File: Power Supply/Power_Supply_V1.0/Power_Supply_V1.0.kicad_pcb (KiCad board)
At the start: 2 copper layers, 158.8 x 67.3 mm, 44 parts

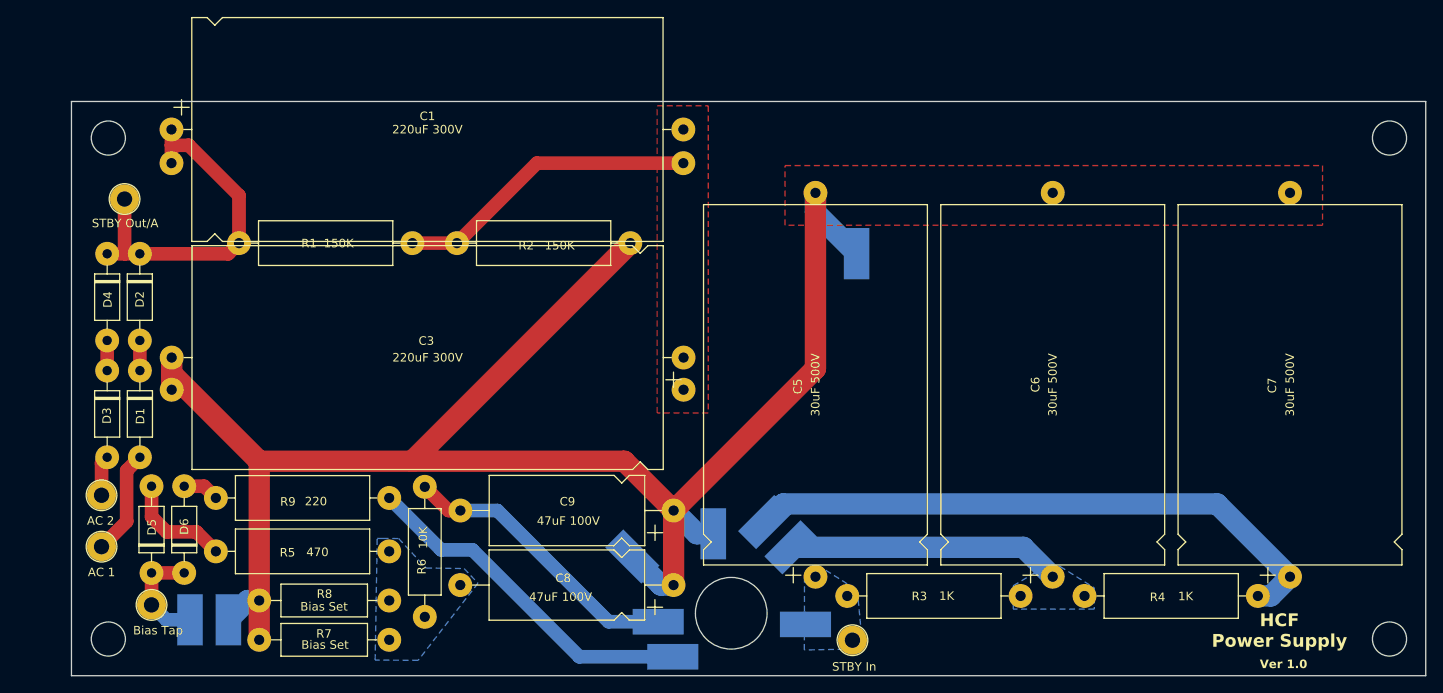
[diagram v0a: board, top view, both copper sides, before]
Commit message: increased trace width
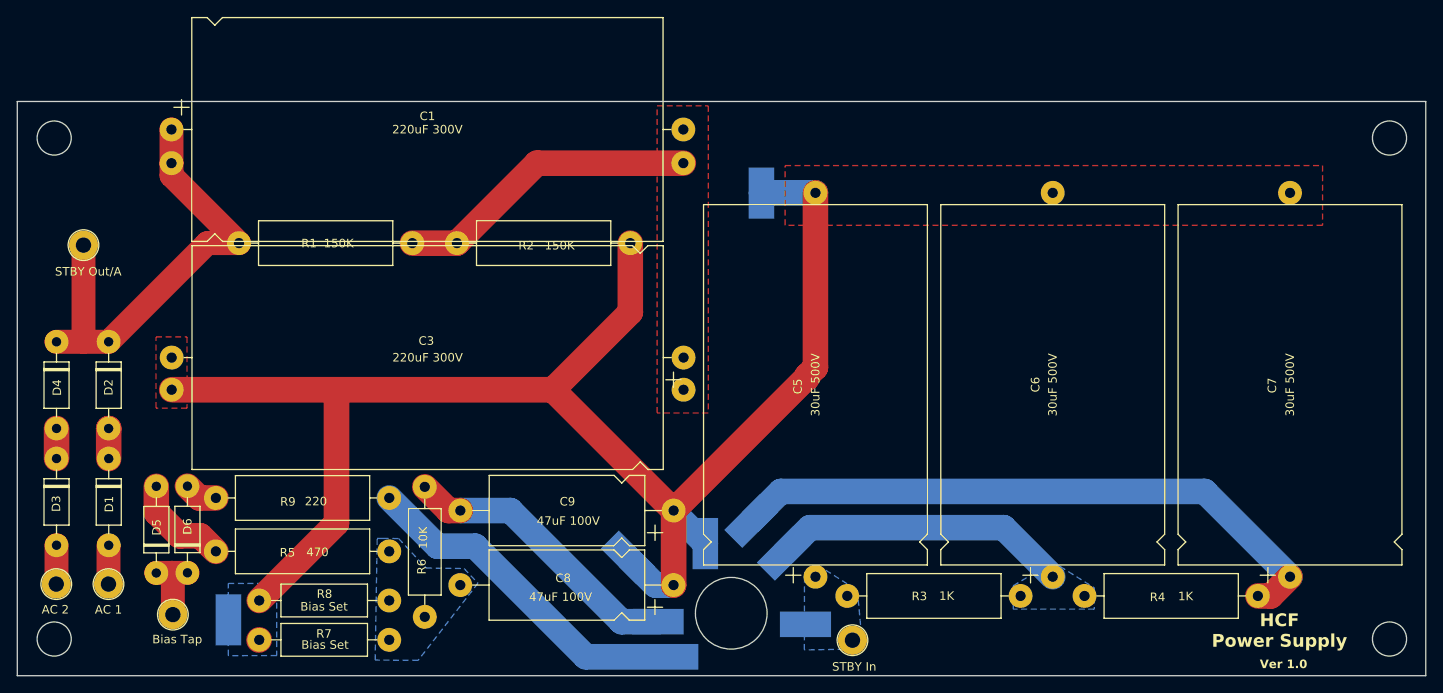
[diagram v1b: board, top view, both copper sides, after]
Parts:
- removed TP15: Bias Tap Out, HiroFootprints:WirePad
- moved TP14 13.2 mm to (142.2, 80.5)
- moved D3 11.9 mm to (59.6, 111.3)
- moved D4 11.9 mm to (59.6, 97.7)
- moved TP11 11.7 mm to (59.6, 126.1)
- moved D1 10.9 mm to (65.7, 111.3)
- moved D2 10.9 mm to (65.7, 97.7)
- moved TP1 7.24 mm to (62.8, 86.3)
- moved REF** 6.35 mm to (59.3, 73.8)
- moved REF** 6.35 mm to (59.3, 132.5)
- moved TP10 4.46 mm to (65.7, 126.1)
- moved TP9 2.75 mm to (73.2, 129.6)
- moved TP5 1.63 mm to (140.9, 118.8)
- moved TP12 1.49 mm to (135.7, 121.1)
- moved TP4 1.14 mm to (144.7, 122.7)
- moved D5 0.56 mm to (71.3, 124.8)
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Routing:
- net GND: track 204.9 -> 185.5 mm
- net Net-(D2-K): track 42.3 -> 54.1 mm
- net Net-(D1-A): track 12.3 -> 4.56 mm
- net 60VAC: track 12.8 -> 8.58 mm
- net C: track 32.1 -> 35.1 mm
- net D: track 70.6 -> 73.4 mm
- net Net-(D5-A): track 12.8 -> 11.9 mm
- added copper zone on B.Cu, net GND
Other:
- board size 158.8 x 67.3 mm -> 165.1 x 67.3 mm

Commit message: updated power supply board with more diode spacing
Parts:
- moved TP1 2.31 mm to (62.3, 88.6)
- moved TP9 0.94 mm to (72.5, 129.0)
- moved D5 0.93 mm to (70.4, 124.7)
- moved D6 0.40 mm to (74.5, 124.8)
- moved D4 0.28 mm to (59.3, 97.6)
- moved TP11 0.28 mm to (59.3, 126.0)
- moved D3 0.28 mm to (59.3, 111.3)
- moved D2 0.28 mm to (65.4, 97.6)
- moved TP10 0.28 mm to (65.4, 126.0)
- moved D1 0.28 mm to (65.5, 111.3)
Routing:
- net Net-(D2-K): track 54.1 -> 52.0 mm
- net Net-(D5-A): track 11.9 -> 13.1 mm
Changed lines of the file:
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@@
 	(footprint "HiroFootprints:Out_Hole_3.4_1.8"
 		(layer "F.Cu")
-		(at 65.69 126.06)
+		(at 65.42 126)
 		(property "Reference" "TP10"
 			(at 0 -0.5 0)
@@
 	(footprint "Diode_THT:D_DO-41_SOD81_P10.16mm_Horizontal"
 		(layer "F.Cu")
-		(at 59.6 97.66 -90)
+		(at 59.33 97.6 -90)
 		(descr "Diode, DO-41_SOD81 series, Axial, Horizontal, pin pitch=10.16mm, , length*diameter=5.2*2.7mm^2, , http://www.diodes.com/_files/packages/DO-41%20(Plastic).pdf")
 		(tags "Diode DO-41_SOD81 series Axial Horizontal pin pitch 10.16mm  length 5.2mm diameter 2.7mm")
@@
 	(footprint "Diode_THT:D_DO-41_SOD81_P10.16mm_Horizontal"
 		(layer "F.Cu")
-		(at 74.945625 124.74 90)
+		(at 74.55 124.75 90)
 		(descr "Diode, DO-41_SOD81 series, Axial, Horizontal, pin pitch=10.16mm, , length*diameter=5.2*2.7mm^2, , http://www.diodes.com/_files/packages/DO-41%20(Plastic).pdf")
 		(tags "Diode DO-41_SOD81 series Axial Horizontal pin pitch 10.16mm  length 5.2mm diameter 2.7mm")
@@
 	(footprint "Diode_THT:D_DO-41_SOD81_P10.16mm_Horizontal"
 		(layer "F.Cu")
-		(at 65.72 111.35 -90)
+		(at 65.45 111.29 -90)
 		(descr "Diode, DO-41_SOD81 series, Axial, Horizontal, pin pitch=10.16mm, , length*diameter=5.2*2.7mm^2, , http://www.diodes.com/_files/packages/DO-41%20(Plastic).pdf")
 		(tags "Diode DO-41_SOD81 series Axial Horizontal pin pitch 10.16mm  length 5.2mm diameter 2.7mm")
@@
 	(footprint "HiroFootprints:Out_Hole_3.4_1.8"
 		(layer "F.Cu")
-		(at 62.76 86.33)
+		(at 62.28 88.59)
 		(property "Reference" "TP1"
 			(at 0 -0.5 0)
@@
 	(footprint "Diode_THT:D_DO-41_SOD81_P10.16mm_Horizontal"
 		(layer "F.Cu")
-		(at 71.3 124.76 90)
+		(at 70.37 124.74 90)
 		(descr "Diode, DO-41_SOD81 series, Axial, Horizontal, pin pitch=10.16mm, , length*diameter=5.2*2.7mm^2, , http://www.diodes.com/_files/packages/DO-41%20(Plastic).pdf")
 		(tags "Diode DO-41_SOD81 series Axial Horizontal pin pitch 10.16mm  length 5.2mm diameter 2.7mm")
@@
 	(footprint "HiroFootprints:Out_Hole_3.4_1.8"
 		(layer "F.Cu")
-		(at 73.24 129.64)
+		(at 72.54 129.02)
 		(property "Reference" "TP9"
 			(at 0 -0.5 0)
@@
 	(footprint "Diode_THT:D_DO-41_SOD81_P10.16mm_Horizontal"
 		(layer "F.Cu")
-		(at 65.71 97.66 -90)
+		(at 65.44 97.6 -90)
 		(descr "Diode, DO-41_SOD81 series, Axial, Horizontal, pin pitch=10.16mm, , length*diameter=5.2*2.7mm^2, , http://www.diodes.com/_files/packages/DO-41%20(Plastic).pdf")
 		(tags "Diode DO-41_SOD81 series Axial Horizontal pin pitch 10.16mm  length 5.2mm diameter 2.7mm")
@@
 	(footprint "HiroFootprints:Out_Hole_3.4_1.8"
 		(layer "F.Cu")
-		(at 59.57 126.06)
+		(at 59.3 126)
 		(property "Reference" "TP11"
 			(at 0 -0.5 0)
@@
 	(footprint "Diode_THT:D_DO-41_SOD81_P10.16mm_Horizontal"
 		(layer "F.Cu")
-		(at 59.6 111.35 -90)
+		(at 59.33 111.29 -90)
 		(descr "Diode, DO-41_SOD81 series, Axial, Horizontal, pin pitch=10.16mm, , length*diameter=5.2*2.7mm^2, , http://www.diodes.com/_files/packages/DO-41%20(Plastic).pdf")
 		(tags "Diode DO-41_SOD81 series Axial Horizontal pin pitch 10.16mm  length 5.2mm diameter 2.7mm")
@@
 	)
 	(segment
-		(start 62.77 97.66)
-		(end 65.71 97.66)
-		(width 2.8)
-		(layer "F.Cu")
-		(net 1)
-	)
-	(segment
-		(start 62.76 86.33)
-		(end 62.76 97.65)
+		(start 62.28 88.59)
+		(end 62.28 97.6)
 		(width 2.8)
 		(layer "F.Cu")
@@
 	)
 	(segment
-		(start 73.075 72.775)
-		(end 73.075 76.72)
+		(start 76.9475 86.0925)
+		(end 65.44 97.6)
 		(width 2.8)
 		(layer "F.Cu")
@@
 	)
 	(segment
-		(start 59.6 97.66)
-		(end 62.77 97.66)
+		(start 62.28 97.6)
+		(end 65.44 97.6)
 		(width 2.8)
 		(layer "F.Cu")
@@
 	)
 	(segment
-		(start 80.99 86.0925)
-		(end 77.2775 86.0925)
+		(start 59.33 97.6)
+		(end 62.28 97.6)
 		(width 2.8)
 		(layer "F.Cu")
@@
 	)
 	(segment
-		(start 73.075 78.1775)
+		(start 73.075 72.775)
 		(end 73.075 76.72)
 		(width 2.8)
@@
 	)
 	(segment
-		(start 62.76 97.65)
-		(end 62.77 97.66)
+		(start 73.075 78.1775)
+		(end 73.075 76.72)
 		(width 2.8)
 		(layer "F.Cu")
@@
 	)
 	(segment
-		(start 77.2775 86.0925)
-		(end 65.71 97.66)
+		(start 80.99 86.0925)
+		(end 76.9475 86.0925)
 		(width 2.8)
 		(layer "F.Cu")
@@
 		(start 115.9125 76.72)
 		(end 133.075 76.72)
-		(width 3)
+		(width 2.8)
 		(layer "F.Cu")
 		(net 2)
@@
 		(start 101.31 86.0925)
 		(end 106.54 86.0925)
-		(width 3)
+		(width 2.8)
 		(layer "F.Cu")
 		(net 2)
@@
 		(start 106.54 86.0925)
 		(end 115.9125 76.72)
-		(width 3)
+		(width 2.8)
 		(layer "F.Cu")
 		(net 2)
@@
 		(start 170.625 119.45)
 		(end 176.375 125.2)
-		(width 3)
+		(width 2.8)
 		(layer "B.Cu")
 		(net 5)
@@
 		(start 144.87 122.48)
 		(end 147.9 119.45)
-		(width 3)
+		(width 2.8)
 		(layer "B.Cu")
 		(net 5)
@@
 		(start 147.9 119.45)
 		(end 170.625 119.45)
-		(width 3)
+		(width 2.8)
 		(layer "B.Cu")
 		(net 5)
@@
 		(start 201.938 127.45)
 		(end 200.42 127.45)
-		(width 3)
+		(width 2.8)
 		(layer "F.Cu")
 		(net 6)
@@
 		(start 204.188 125.2)
 		(end 201.938 127.45)
-		(width 3)
+		(width 2.8)
 		(layer "F.Cu")
 		(net 6)
@@
 		(start 194.188 115.2)
 		(end 204.188 125.2)
-		(width 3)
+		(width 2.8)
 		(layer "B.Cu")
 		(net 6)
@@
 		(start 141.046777 118.653223)
 		(end 144.5 115.2)
-		(width 3)
+		(width 2.8)
 		(layer "B.Cu")
 		(net 6)
@@
 		(start 144.5 115.2)
 		(end 194.188 115.2)
-		(width 3)
+		(width 2.8)
 		(layer "B.Cu")
 		(net 6)
@@
 		(start 105.54825 117.44)
 		(end 106.937 117.44)
-		(width 3)
+		(width 2.8)
 		(layer "F.Cu")
 		(net 8)
@@
 		(start 102.76825 114.66)
 		(end 105.54825 117.44)
-		(width 3)
+		(width 2.8)
 		(layer "F.Cu")
 		(net 8)
@@
 		(start 125.84 130.47)
 		(end 130.13 130.47)
-		(width 3)
+		(width 2.8)
 		(layer "B.Cu")
 		(net 8)
@@
 		(start 106.937 117.44)
 		(end 112.81 117.44)
-		(width 3)
+		(width 2.8)
 		(layer "B.Cu")
 		(net 8)
@@
 		(start 112.81 117.44)
 		(end 125.84 130.47)
-		(width 3)
+		(width 2.8)
 		(layer "B.Cu")
 		(net 8)
 	)
 	(segment
-		(start 65.72 107.83)
-		(end 65.71 107.82)
-		(width 3)
+		(start 65.45 107.77)
+		(end 65.44 107.76)
+		(width 2.8)
 		(layer "F.Cu")
 		(net 9)
 	)
 	(segment
-		(start 65.72 111.35)
-		(end 65.72 107.83)
-		(width 3)
+		(start 65.45 111.29)
+		(end 65.45 107.77)
+		(width 2.8)
 		(layer "F.Cu")
 		(net 9)
 	)
 	(segment
-		(start 65.69 121.54)
-		(end 65.72 121.51)
-		(width 0.2)
+		(start 65.42 121.48)
+		(end 65.45 121.45)
+		(width 2.8)
 		(layer "F.Cu")
 		(net 10)
 	)
 	(segment
-		(start 65.69 126.06)
-		(end 65.69 121.54)
+		(start 65.42 126)
+		(end 65.42 121.48)
 		(width 2.8)
 		(layer "F.Cu")
@@
 	)
 	(segment
-		(start 59.6 121.51)
-		(end 59.6 126.03)
+		(start 59.33 121.45)
+		(end 59.33 125.97)
 		(width 2.8)
 		(layer "F.Cu")
@@
 	)
 	(segment
-		(start 59.6 126.03)
-		(end 59.57 126.06)
-		(width 0.2)
+		(start 59.33 125.97)
+		(end 59.3 126)
+		(width 2.8)
 		(layer "F.Cu")
 		(net 11)
 	)
 	(segment
-		(start 59.6 107.82)
-		(end 59.6 111.35)
-		(width 3)
+		(start 59.33 107.76)
+		(end 59.33 111.29)
+		(width 2.8)
 		(layer "F.Cu")
 		(net 12)
 	)
 	(segment
-		(start 71.3 117.65)
-		(end 74.06 120.41)
-		(width 3)
+		(start 75.5045 119.45)
+		(end 78.2795 122.225)
+		(width 2.8)
 		(layer "F.Cu")
 		(net 13)
 	)
 	(segment
-		(start 74.06 120.41)
-		(end 76.4645 120.41)
-		(width 3)
+		(start 70.37 114.58)
+		(end 70.37 118)
+		(width 2.8)
 		(layer "F.Cu")
 		(net 13)
 	)
 	(segment
-		(start 76.4645 120.41)
-		(end 78.2795 122.225)
-		(width 3)
+		(start 71.82 119.45)
+		(end 75.5045 119.45)
+		(width 2.8)
 		(layer "F.Cu")
 		(net 13)
 	)
 	(segment
-		(start 71.3 114.6)
-		(end 71.3 117.65)
-		(width 3)
+		(start 70.37 118)
+		(end 71.82 119.45)
+		(width 2.8)
 		(layer "F.Cu")
 		(net 13)
 	)
 	(segment
-		(start 73.24 124.81)
-		(end 73.17 124.74)
+		(start 74.54 124.74)
+		(end 74.55 124.75)
 		(width 2.8)
 		(layer "F.Cu")
@@
 	)
 	(segment
-		(start 71.32 124.74)
-		(end 71.3 124.76)
+		(start 72.54 129.02)
+		(end 72.54 124.75)
 		(width 2.8)
 		(layer "F.Cu")
@@
 	)
 	(segment
-		(start 73.24 129.64)
-		(end 73.24 124.81)
+		(start 72.54 124.75)
+		(end 72.55 124.74)
 		(width 2.8)
 		(layer "F.Cu")
@@
 	)
 	(segment
-		(start 74.945625 124.74)
-		(end 73.17 124.74)
+		(start 72.55 124.74)
+		(end 74.54 124.74)
 		(width 2.8)
 		(layer "F.Cu")
@@
 	)
 	(segment
-		(start 73.17 124.74)
-		(end 71.32 124.74)
+		(start 70.37 124.74)
+		(end 72.55 124.74)
 		(width 2.8)
 		(layer "F.Cu")
@@
 	)
 	(segment
-		(start 74.945625 114.58)
-		(end 76.330625 115.965)
-		(width 3)
+		(start 76.9045 114.59)
+		(end 78.2795 115.965)
+		(width 2.8)
 		(layer "F.Cu")
 		(net 15)
 	)
 	(segment
-		(start 76.330625 115.965)
-		(end 78.2795 115.965)
-		(width 3)
+		(start 74.55 114.59)
+		(end 76.9045 114.59)
+		(width 2.8)
 		(layer "F.Cu")
 		(net 15)
@@
 		(start 104.2545 121.62)
 		(end 108.68 121.62)
-		(width 3)
+		(width 2.8)
 		(layer "B.Cu")
 		(net 16)
@@
 		(start 108.68 121.62)
 		(end 121.64 134.58)
-		(width 3)
+		(width 2.8)
 		(layer "B.Cu")
 		(net 16)
@@
 		(start 98.5995 115.965)
 		(end 104.2545 121.62)
-		(width 3)
+		(width 2.8)
 		(layer "B.Cu")
 		(net 16)
@@
 		(start 121.64 134.58)
 		(end 131.83 134.58)
-		(width 3)
+		(width 2.8)
 		(layer "B.Cu")
 		(net 16)

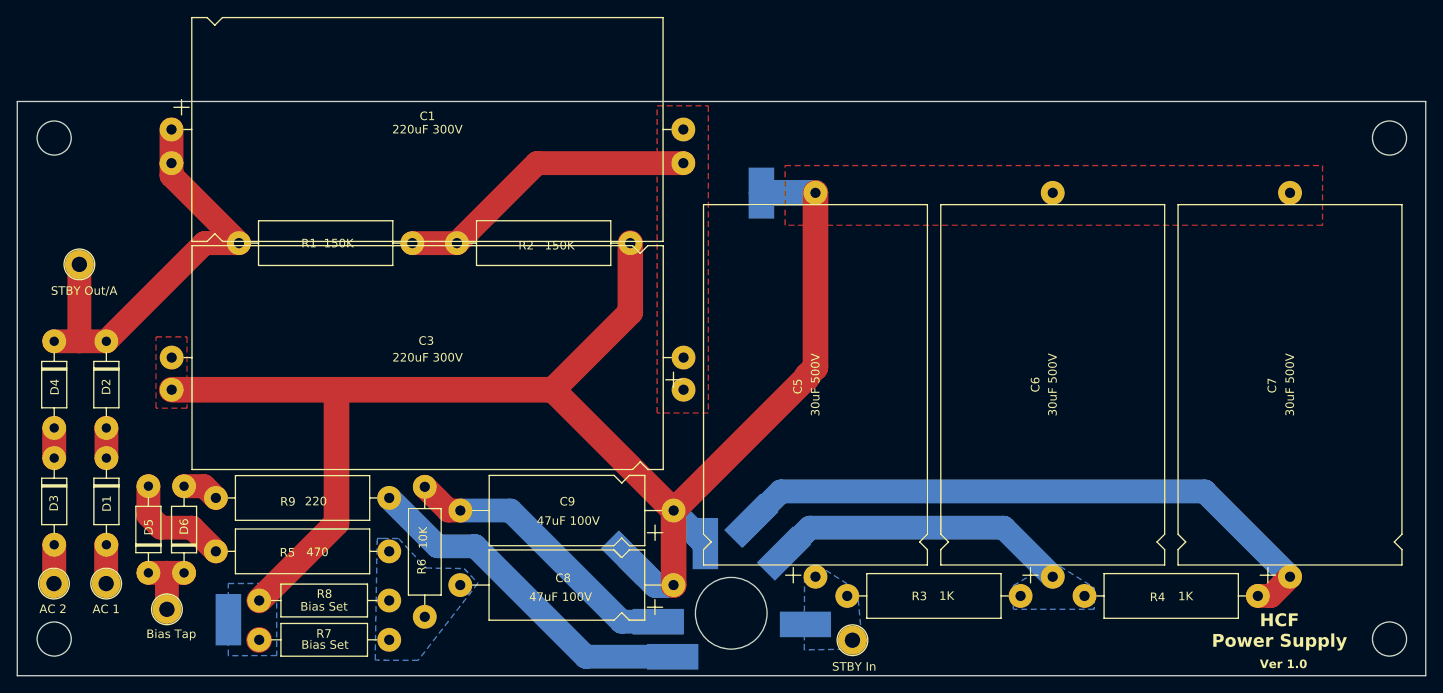
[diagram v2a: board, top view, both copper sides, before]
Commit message: improved grounding trace size and scheme for power supply
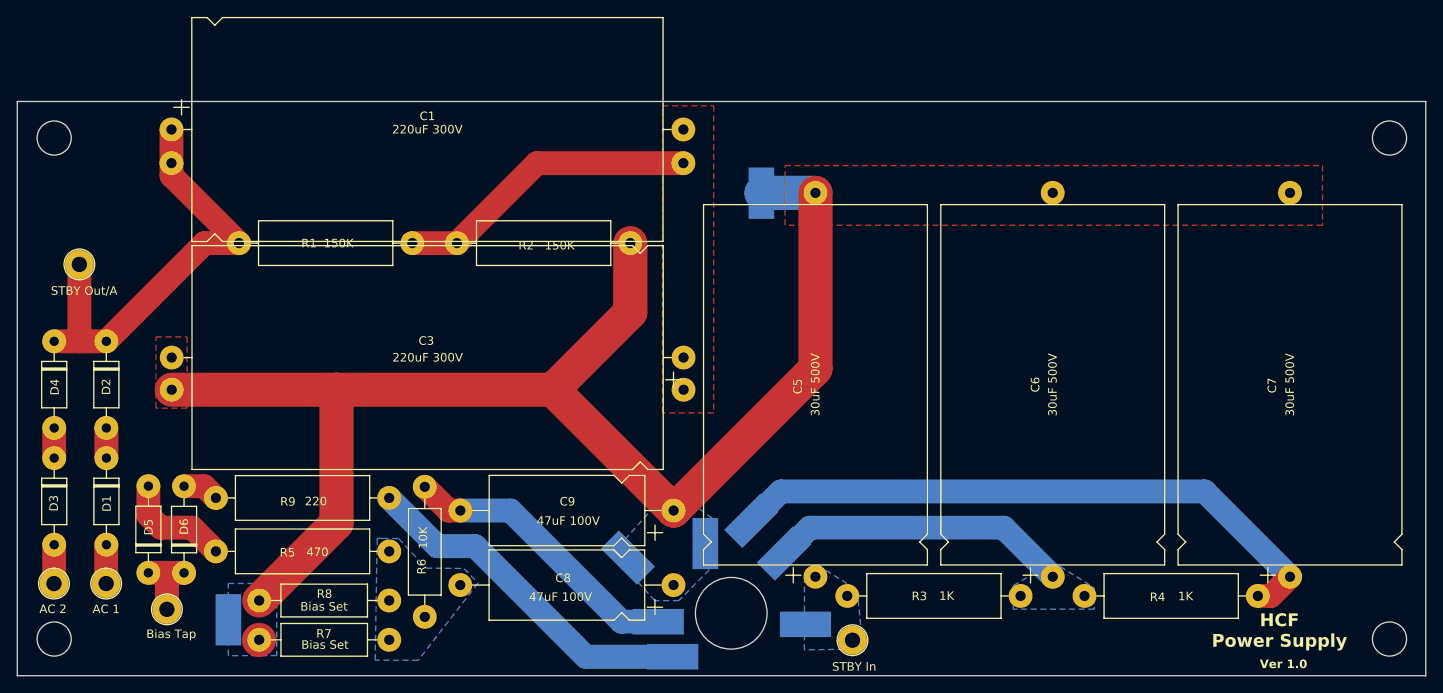
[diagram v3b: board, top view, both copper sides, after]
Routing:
- net GND: track 185.5 -> 164.6 mm
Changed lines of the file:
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@@
 			(net 3 "GND")
 			(pintype "passive")
+			(zone_connect 2)
 		)
 		(pad "2" thru_hole circle
@@
 			(net 3 "GND")
 			(pintype "passive")
+			(zone_connect 2)
 		)
 		(pad "2" thru_hole circle
@@
 			(pinfunction "1")
 			(pintype "passive")
+			(zone_connect 2)
 		)
 		(embedded_fonts no)
@@
 			(pinfunction "1")
 			(pintype "passive")
+			(zone_connect 2)
 		)
 		(embedded_fonts no)
@@
 	)
 	(segment
-		(start 131.937 117.44)
-		(end 131.937 126.163)
-		(width 3)
-		(layer "F.Cu")
-		(net 3)
-	)
-	(segment
 		(start 126.86 94.197)
 		(end 117.777 103.28)
-		(width 3)
+		(width 4)
 		(layer "F.Cu")
 		(net 3)
@@
 		(start 73.1 103.28)
 		(end 92.42 103.28)
-		(width 3)
+		(width 4)
 		(layer "F.Cu")
 		(net 3)
 	)
 	(segment
-		(start 147.57 101.66)
-		(end 148.562 100.668)
-		(width 3)
+		(start 148.562 80.2)
+		(end 148.562 100.815)
+		(width 4)
 		(layer "F.Cu")
 		(net 3)
@@
 		(start 92.42 103.28)
 		(end 117.777 103.28)
-		(width 3)
-		(layer "F.Cu")
-		(net 3)
-	)
-	(segment
-		(start 147.477 101.9)
-		(end 147.57 101.9)
-		(width 3)
+		(width 4)
 		(layer "F.Cu")
 		(net 3)
@@
 		(start 117.777 103.28)
 		(end 131.937 117.44)
-		(width 3)
+		(width 4)
 		(layer "F.Cu")
 		(net 3)
@@
 		(start 92.42 118.9245)
 		(end 83.3595 127.985)
-		(width 3)
+		(width 4)
 		(layer "F.Cu")
 		(net 3)
 	)
 	(segment
-		(start 131.937 126.163)
-		(end 131.925 126.175)
-		(width 3)
-		(layer "F.Cu")
-		(net 3)
-	)
-	(segment
-		(start 131.937 117.44)
-		(end 147.477 101.9)
-		(width 3)
-		(layer "F.Cu")
-		(net 3)
-	)
-	(segment
-		(start 147.57 101.9)
-		(end 147.57 101.66)
-		(width 3)
+		(start 148.562 100.815)
+		(end 131.937 117.44)
+		(width 4)
 		(layer "F.Cu")
 		(net 3)
@@
 		(start 126.86 86.0925)
 		(end 126.86 94.197)
-		(width 3)
+		(width 4)
 		(layer "F.Cu")
 		(net 3)
@@
 		(start 83.3295 132.625)
 		(end 83.3595 132.595)
-		(width 3)
+		(width 4)
 		(layer "F.Cu")
 		(net 3)
@@
 		(start 92.42 103.28)
 		(end 92.42 118.9245)
-		(width 3)
+		(width 4)
 		(layer "F.Cu")
 		(net 3)
 	)
 	(segment
-		(start 148.562 100.668)
-		(end 148.562 80.2)
-		(width 3)
-		(layer "F.Cu")
-		(net 3)
-	)
-	(segment
-		(start 131.937 117.44)
-		(end 131.937 117.597)
-		(width 3)
-		(layer "B.Cu")
-		(net 3)
-	)
-	(segment
-		(start 131.937 117.597)
-		(end 135.65 121.31)
-		(width 3)
-		(layer "B.Cu")
-		(net 3)
-	)
-	(segment
 		(start 142.26 80.2)
 		(end 142.23 80.23)
-		(width 3)
-		(layer "B.Cu")
-		(net 3)
-	)
-	(segment
-		(start 131.925 126.175)
-		(end 129.795 126.175)
-		(width 3)
+		(width 4)
 		(layer "B.Cu")
 		(net 3)
@@
 		(start 148.562 80.2)
 		(end 142.26 80.2)
-		(width 3)
-		(layer "B.Cu")
-		(net 3)
-	)
-	(segment
-		(start 129.795 126.175)
-		(end 126.573223 122.953223)
-		(width 3)
+		(width 4)
 		(layer "B.Cu")
 		(net 3)
@@
 		(polygon
 			(pts
-				(xy 130 70) (xy 136 70) (xy 136 106) (xy 130 106)
+				(xy 130.63 70) (xy 136.63 70) (xy 136.63 106) (xy 130.63 106)
 			)
 		)
@@
 			)
 		)
+	)
+	(zone
+		(net 3)
+		(net_name "GND")
+		(layer "B.Cu")
+		(hatch edge 0.5)
+		(priority 7)
+		(connect_pads
+			(clearance 0.5)
+		)
+		(min_thickness 0.25)
+		(filled_areas_thickness no)
+		(fill yes
+			(thermal_gap 0.5)
+			(thermal_bridge_width 0.5)
+		)
+		(polygon
+			(pts
+				(xy 133.185929 115.89) (xy 136.915929 118.7) (xy 136.905929 123.59) (xy 132.545929 128) (xy 129.745929 128)
+				(xy 124.725929 122.54) (xy 130.625929 115.89)
+			)
+		)
